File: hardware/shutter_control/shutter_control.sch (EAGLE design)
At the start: 32 parts, among them IC1 MEGA168/328, IC2 RFM12, IC3 LP2950Z, K1 G6D-1A-ASI5VDC, K2 G6D-1A-ASI5VDC, T1 BC547, T2 BC547, T3 BC547, X1 SW Out

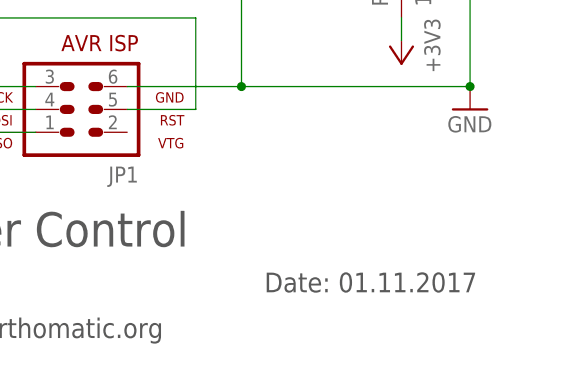
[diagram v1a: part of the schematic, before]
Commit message: Change schematics date.
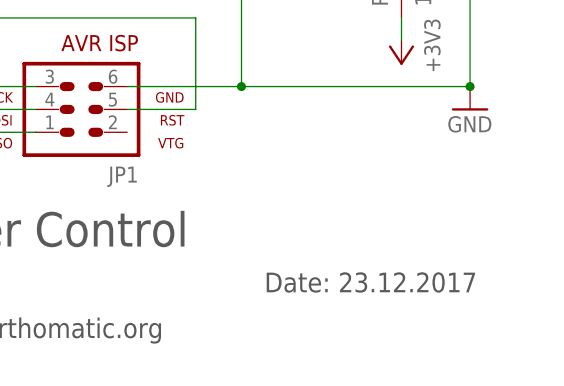
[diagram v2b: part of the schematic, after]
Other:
- note added: "Date: 23.12.2017"
- note removed: "Date: 01.11.2017"
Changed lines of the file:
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@@
 <?xml version="1.0" encoding="utf-8"?>
 <!DOCTYPE eagle SYSTEM "eagle.dtd">
-<eagle version="7.1.0">
+<eagle version="7.3.0">
 <drawing>
 <settings>
@@
 <frame x1="-66.04" y1="-55.88" x2="132.08" y2="96.52" columns="8" rows="5" layer="97"/>
 <text x="17.78" y="-33.02" size="3.81" layer="97">smarthomatic Shutter Control</text>
-<text x="96.52" y="-38.1" size="2.1844" layer="97">Date: 01.11.2017</text>
+<text x="96.52" y="-38.1" size="2.1844" layer="97">Date: 23.12.2017</text>
 <text x="17.78" y="-38.1" size="2.1844" layer="97">Rev 1.0</text>
 <text x="17.78" y="-43.18" size="2.1844" layer="97">Copyright (c) Uwe Freese, www.smarthomatic.org</text>
